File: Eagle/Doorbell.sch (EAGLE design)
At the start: 31 parts, among them U1 MIC2920A-3.3

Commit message: r1 - switching supply
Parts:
- removed C5: 470uF 25V, SparkFun-Capacitors:CAP_POLE
- removed U1: MIC2920A-3.3, Microchip_By_element14_Batch_1:MCP1790-3302E/DB
- added C8: 2.2uF, SparkFun-Passives:CAP1206
- added D5: BAT20J, SparkFun-DiscreteSemi:DIODE-SCHOTTKY-BAT20J
- added L1: 6.8uH, SparkFun-Passives:INDUCTOR1007
- added VREG: LMR16006YQ3DDCRQ1, CuriousTech:LMR16006YQ
- C1: value 0.1uF -> 10uF
- C4: value 10uF 16V -> 100uF; device SparkFun-Capacitors:CAP_POLC -> SparkFun-Passives:CAP_POLF80
- R4: value 5K6 -> 470
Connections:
- removed net N$1: C3.1, C5.+, C6.1, D1.C, D3.C, U1.VIN
- new net +24V: C3.1, C4.+, C8.1, D1.C, D3.C, VREG.VIN
- new net N$10: C6.2, VREG.CB
- new net N$7: C6.1, D5.C, L1.1, VREG.SW
- net 3V3: now also L1.2, VREG.FB; no longer C4.+, U1.VOUT
- net GND: now also C8.2, D5.A, VREG.GND; no longer C5.-, C6.2, U1.GND_(TAB), U1.GND_(TAB)_2
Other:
- moved on the sheet: C1, C4, C6, C7

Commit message: Add files via upload
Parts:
- removed X1: (no value), con-molex:KK-156-4
- added 3V3: MCP1755T-3302E/OT, Microchip_By_element14_Batch_1:MCP1801T-3302I/OT
- added C5: 0.1uF, SparkFun-Capacitors:CAP
- added D6, D7: (no value), SparkFun-DiscreteSemi:DIODESOD123
- added J2, J3: (no value), SparkFun-Connectors:M01SMDNS
- added L2: (no value), SparkFun-Passives:INDUCTOR0805
- added Q1: MOSFET-NCHANNEL, SparkFun-DiscreteSemi:MOSFET-NCHANNELAO3404A
- added R9: 1K, SparkFun-Resistors:RESISTOR0805-RES
- added U$6, U$7: SMD-PAD-SM, CuriousTech:SMD-PAD-SM
- added X2: 1751251, con-phoenix-350:1751251
- C1: value 10uF -> (none); device SparkFun-Capacitors:CAP -> SparkFun-Capacitors:CAP_POLPTH4
- C2: value 1uF -> 2.2uF; device SparkFun-Capacitors:CAP -> SparkFun-Passives:CAP1206
- C3: value 0.1uF -> 10uF
- C4: value 100uF -> 0.1uF; device SparkFun-Passives:CAP_POLF80 -> SparkFun-Capacitors:CAP
- C8: value 2.2uF -> 1uF; device SparkFun-Passives:CAP1206 -> SparkFun-Capacitors:CAP
- L1: value 6.8uH -> (none); device SparkFun-Passives:INDUCTOR1007 -> SparkFun-Passives:INDUCTOR0805
- R4: value 470 -> 1K
- R5, R6: value 10K -> 4K7
- VREG: value LMR16006YQ3DDCRQ1 -> LMR16006YQ5DDCRQ1
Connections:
- net IO5 renamed DB
- new net 5V: 3V3.VIN, 3V3.~SHDN, C3.1, C7.1, D6.C, L1.2, L2.2, U$7.P$1, VREG.FB, _.8
- new net N$1: D6.A, D7.A, Q1.D, U$6.P$1
- new net N$8: Q1.G, R9.2
- net +24V: now also C1.+, C2.1, C4.1, D7.C, U$3.P$1; no longer C3.1, C4.+, C8.1
- net 3V3: now also 3V3.VOUT, C5.1, _.7; no longer C1.1, C7.1, L1.2, U$3.P$1, VREG.FB, _.6, _.8
- net GND: now also 3V3.VSS, C1.-, C2.2, C4.2, C5.2, Q1.S, _.3; no longer C1.2, C4.-, C8.2, _.7
- net IO12: now also _.5; no longer _.4
- net IO13: now also _.6; no longer _.5
- net IO14: now also _.4; no longer _.3
- net IO15: now also R9.1
- net J1: now also C8.2, X2-2.K; no longer C2.2, X1-3.S
- net N$2: now also C8.1; no longer C2.1
- net N$3: now also J2.1, X2-1.K; no longer X1-1.S, X1-2.S
- net N$5: now also J3.1, X2-3.K; no longer X1-4.S
- net N$7: now also L2.1
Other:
- note added: "<--- 100-200 ohm, 5W resistor --->"
- note added: "<-Use only one!->"
- moved on the sheet: ., C2, C3, C6, C7, C8, D1, D2, D3, D4, D5, DS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

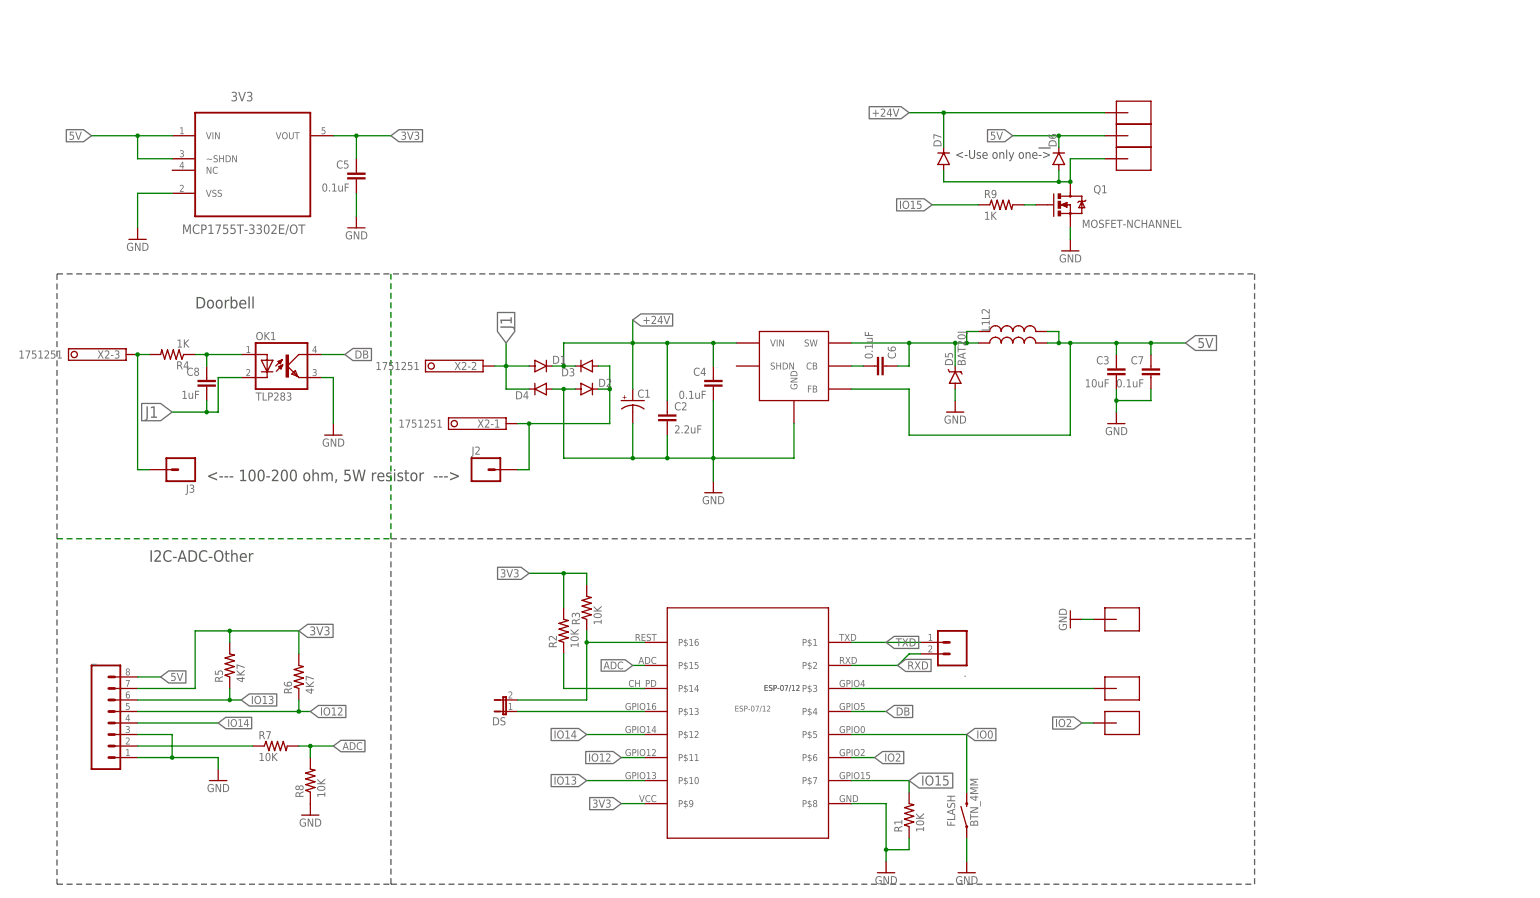
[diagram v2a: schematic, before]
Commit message: Added the inline diode
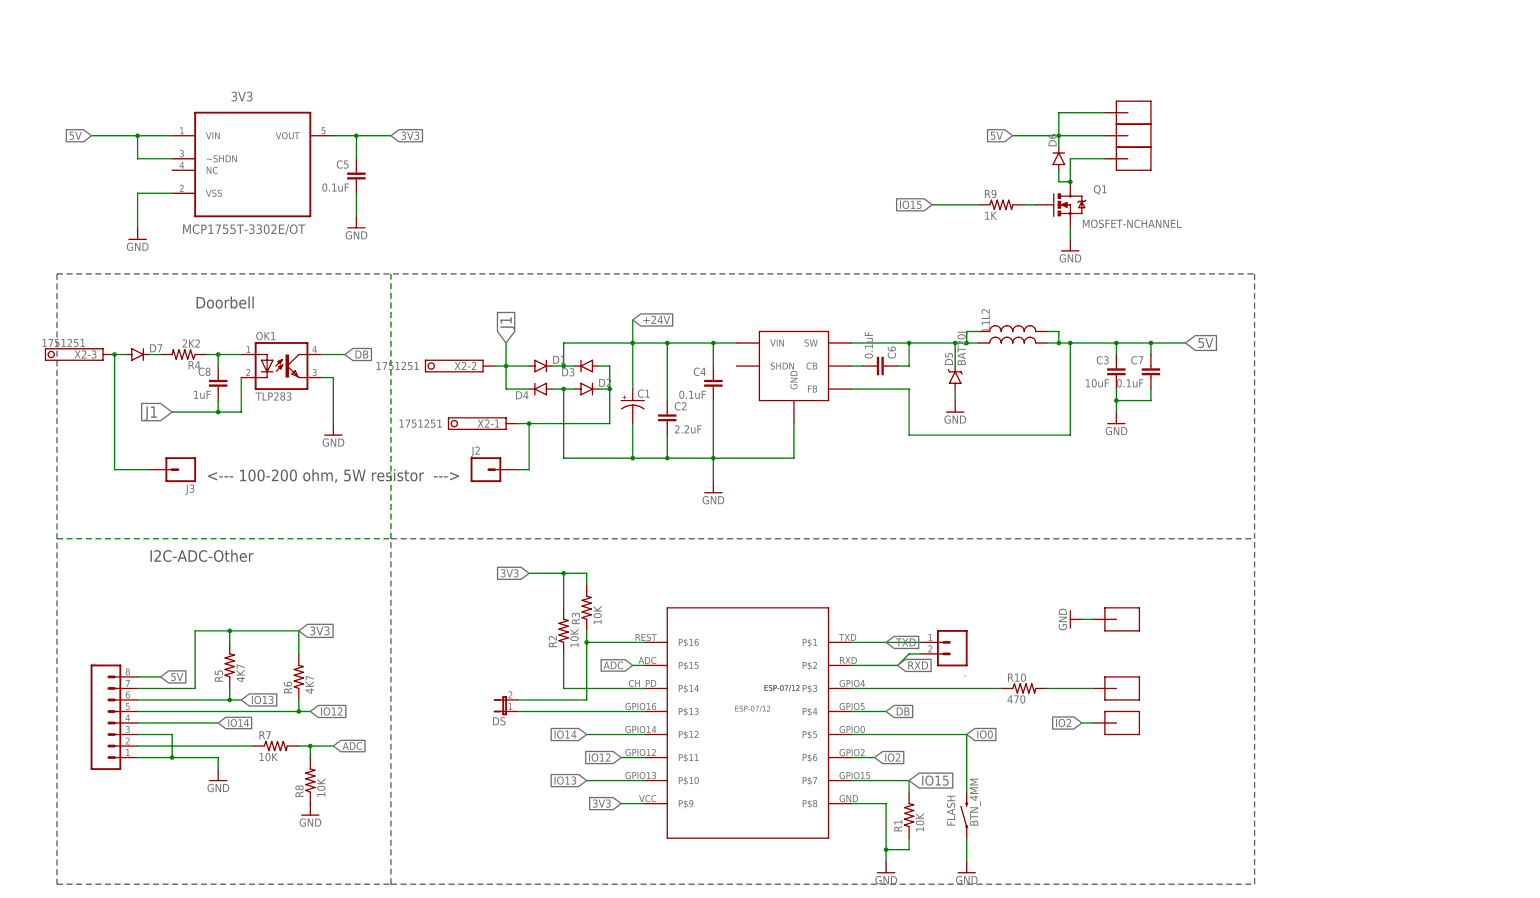
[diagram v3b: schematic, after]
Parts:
- added R10: 470, SparkFun-Resistors:RESISTOR0805-RES
- R4: value 1K -> 2K2
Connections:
- new net N$12: R10.2, U$2.P$1
- new net N$13: D7.C, R4.2
- net +24V: no longer D7.C, U$3.P$1
- net 5V: now also U$3.P$1
- net N$1: no longer D7.A
- net N$5: now also D7.A; no longer R4.2
- net N$6: now also R10.1; no longer U$2.P$1
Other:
- note removed: "<-Use only one!->"
- moved on the sheet: C8, D7, R4, X2-3
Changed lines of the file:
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@@
 <part name="C4" library="SparkFun-Capacitors" deviceset="CAP" device="" value="0.1uF"/>
 <part name="GND7" library="supply1" deviceset="GND" device=""/>
-<part name="R4" library="SparkFun-Resistors" deviceset="RESISTOR" device="0805-RES" value="1K"/>
+<part name="R4" library="SparkFun-Resistors" deviceset="RESISTOR" device="0805-RES" value="2K2"/>
 <part name="FLASH" library="CuriousTech" deviceset="BTN_4MM" device=""/>
 <part name="GND3" library="supply1" deviceset="GND" device=""/>
@@
 <part name="J3" library="SparkFun-Connectors" deviceset="M01" device="SMDNS"/>
 <part name="D6" library="SparkFun-DiscreteSemi" deviceset="DIODE" device="SOD123"/>
-<part name="D7" library="SparkFun-DiscreteSemi" deviceset="DIODE" device="SOD123"/>
 <part name="U$3" library="CuriousTech" deviceset="SMD-PAD-SM" device=""/>
 <part name="C8" library="SparkFun-Capacitors" deviceset="CAP" device="" value="1uF"/>
+<part name="R10" library="SparkFun-Resistors" deviceset="RESISTOR" device="0805-RES" value="470"/>
+<part name="D7" library="SparkFun-DiscreteSemi" deviceset="DIODE" device="SOD123"/>
 </parts>
 <sheets>
@@
 <text x="20.32" y="71.12" size="2.54" layer="97" font="vector">I2C-ADC-Other</text>
 <text x="30.48" y="127" size="2.54" layer="97">Doorbell</text>
-<text x="198.12" y="160.02" size="1.9304" layer="97">&lt;-Use only one!-&gt;</text>
 <text x="33.02" y="88.9" size="2.54" layer="97">&lt;--- 100-200 ohm, 5W resistor  ---&gt;</text>
 </plain>
@@
 <attribute name="VALUE" x="38.1" y="20.32" size="1.778" layer="96" rot="MR0"/>
 </instance>
-<instance part="R4" gate="G$1" x="25.4" y="116.84" smashed="yes" rot="R180">
-<attribute name="NAME" x="29.21" y="115.3414" size="1.778" layer="95" rot="R180"/>
-<attribute name="VALUE" x="29.21" y="120.142" size="1.778" layer="96" rot="R180"/>
+<instance part="R4" gate="G$1" x="27.94" y="116.84" smashed="yes" rot="R180">
+<attribute name="NAME" x="31.75" y="115.3414" size="1.778" layer="95" rot="R180"/>
+<attribute name="VALUE" x="31.75" y="120.142" size="1.778" layer="96" rot="R180"/>
 </instance>
 <instance part="FLASH" gate="G$1" x="200.66" y="15.24" smashed="yes" rot="R90">
@@
 <attribute name="VALUE" x="80.01" y="115.189" size="1.778" layer="96" rot="R180"/>
 </instance>
-<instance part="X2" gate="-3" x="15.24" y="116.84" smashed="yes" rot="R180">
-<attribute name="NAME" x="13.97" y="117.729" size="1.778" layer="95" rot="R180"/>
-<attribute name="VALUE" x="1.27" y="117.729" size="1.778" layer="96" rot="R180"/>
+<instance part="X2" gate="-3" x="10.16" y="116.84" smashed="yes" rot="R180">
+<attribute name="NAME" x="8.89" y="117.729" size="1.778" layer="95" rot="R180"/>
+<attribute name="VALUE" x="6.35" y="120.269" size="1.778" layer="96" rot="R180"/>
 </instance>
 <instance part="Q1" gate="G$1" x="223.52" y="149.86" smashed="yes">
@@
 <attribute name="VALUE" x="223.2914" y="162.56" size="1.778" layer="96" rot="R90"/>
 </instance>
-<instance part="D7" gate="G$1" x="195.58" y="160.02" smashed="yes" rot="R90">
-<attribute name="NAME" x="195.0974" y="162.56" size="1.778" layer="95" rot="R90"/>
-<attribute name="VALUE" x="197.8914" y="162.56" size="1.778" layer="96" rot="R90"/>
-</instance>
 <instance part="U$3" gate="G$1" x="236.22" y="170.18" smashed="yes"/>
-<instance part="C8" gate="G$1" x="33.02" y="109.22" smashed="yes" rot="MR0">
-<attribute name="NAME" x="31.496" y="112.141" size="1.778" layer="95" rot="MR0"/>
-<attribute name="VALUE" x="31.496" y="107.061" size="1.778" layer="96" rot="MR0"/>
+<instance part="C8" gate="G$1" x="35.56" y="109.22" smashed="yes" rot="MR0">
+<attribute name="NAME" x="34.036" y="112.141" size="1.778" layer="95" rot="MR0"/>
+<attribute name="VALUE" x="34.036" y="107.061" size="1.778" layer="96" rot="MR0"/>
+</instance>
+<instance part="R10" gate="G$1" x="213.36" y="43.18" smashed="yes">
+<attribute name="NAME" x="209.55" y="44.6786" size="1.778" layer="95"/>
+<attribute name="VALUE" x="209.55" y="39.878" size="1.778" layer="96"/>
+</instance>
+<instance part="D7" gate="G$1" x="17.78" y="116.84" smashed="yes">
+<attribute name="NAME" x="20.32" y="117.3226" size="1.778" layer="95"/>
+<attribute name="VALUE" x="20.32" y="114.5286" size="1.778" layer="96"/>
 </instance>
 </instances>
@@
 <label x="127" y="124.46" size="1.778" layer="95" xref="yes"/>
 </segment>
-<segment>
-<pinref part="D7" gate="G$1" pin="C"/>
-<wire x1="195.58" y1="162.56" x2="195.58" y2="170.18" width="0.1524" layer="91"/>
-<label x="187.96" y="170.18" size="1.778" layer="95" rot="R180" xref="yes"/>
-<pinref part="U$3" gate="G$1" pin="P$1"/>
-<wire x1="195.58" y1="170.18" x2="187.96" y2="170.18" width="0.1524" layer="91"/>
-<wire x1="231.14" y1="170.18" x2="195.58" y2="170.18" width="0.1524" layer="91"/>
-<junction x="195.58" y="170.18"/>
-</segment>
 </net>
 <net name="N$3" class="0">
@@
 <net name="N$5" class="0">
 <segment>
-<pinref part="R4" gate="G$1" pin="2"/>
-<wire x1="17.78" y1="116.84" x2="20.32" y2="116.84" width="0.1524" layer="91"/>
 <pinref part="X2" gate="-3" pin="K"/>
 <pinref part="J3" gate="G$1" pin="1"/>
-<wire x1="20.32" y1="91.44" x2="17.78" y2="91.44" width="0.1524" layer="91"/>
-<wire x1="17.78" y1="91.44" x2="17.78" y2="116.84" width="0.1524" layer="91"/>
-<junction x="17.78" y="116.84"/>
+<wire x1="20.32" y1="91.44" x2="12.7" y2="91.44" width="0.1524" layer="91"/>
+<wire x1="12.7" y1="91.44" x2="12.7" y2="116.84" width="0.1524" layer="91"/>
+<pinref part="D7" gate="G$1" pin="A"/>
+<wire x1="12.7" y1="116.84" x2="15.24" y2="116.84" width="0.1524" layer="91"/>
+<junction x="12.7" y="116.84"/>
 </segment>
 </net>
@@
 </segment>
 <segment>
-<wire x1="40.64" y1="111.76" x2="35.56" y2="111.76" width="0.1524" layer="91"/>
-<wire x1="35.56" y1="111.76" x2="35.56" y2="104.14" width="0.1524" layer="91"/>
-<wire x1="35.56" y1="104.14" x2="33.02" y2="104.14" width="0.1524" layer="91"/>
+<wire x1="40.64" y1="111.76" x2="40.64" y2="104.14" width="0.1524" layer="91"/>
+<wire x1="40.64" y1="104.14" x2="35.56" y2="104.14" width="0.1524" layer="91"/>
 <label x="25.4" y="104.14" size="2.54" layer="95" rot="R180" xref="yes"/>
 <pinref part="OK1" gate="G$1" pin="C"/>
 <pinref part="C8" gate="G$1" pin="2"/>
-<wire x1="33.02" y1="104.14" x2="25.4" y2="104.14" width="0.1524" layer="91"/>
-<wire x1="33.02" y1="106.68" x2="33.02" y2="104.14" width="0.1524" layer="91"/>
-<junction x="33.02" y="104.14"/>
+<wire x1="35.56" y1="104.14" x2="25.4" y2="104.14" width="0.1524" layer="91"/>
+<wire x1="35.56" y1="106.68" x2="35.56" y2="104.14" width="0.1524" layer="91"/>
+<junction x="35.56" y="104.14"/>
 </segment>
 </net>
@@
 <segment>
 <pinref part="R4" gate="G$1" pin="1"/>
-<wire x1="30.48" y1="116.84" x2="33.02" y2="116.84" width="0.1524" layer="91"/>
+<wire x1="33.02" y1="116.84" x2="35.56" y2="116.84" width="0.1524" layer="91"/>
 <pinref part="OK1" gate="G$1" pin="A"/>
 <pinref part="C8" gate="G$1" pin="1"/>
-<wire x1="33.02" y1="116.84" x2="40.64" y2="116.84" width="0.1524" layer="91"/>
-<wire x1="33.02" y1="114.3" x2="33.02" y2="116.84" width="0.1524" layer="91"/>
-<junction x="33.02" y="116.84"/>
+<wire x1="35.56" y1="116.84" x2="40.64" y2="116.84" width="0.1524" layer="91"/>
+<wire x1="35.56" y1="114.3" x2="35.56" y2="116.84" width="0.1524" layer="91"/>
+<junction x="35.56" y="116.84"/>
 </segment>
 </net>
@@
 <wire x1="129.54" y1="48.26" x2="127" y2="48.26" width="0.1524" layer="91"/>
 <label x="127" y="48.26" size="1.6764" layer="95" rot="R180" xref="yes"/>
-</segment>
-</net>
-<net name="N$6" class="0">
-<segment>
-<pinref part="U$1" gate="G$1" pin="P$3"/>
-<wire x1="175.26" y1="43.18" x2="228.6" y2="43.18" width="0.1524" layer="91"/>
-<pinref part="U$2" gate="G$1" pin="P$1"/>
 </segment>
 </net>
@@
 <wire x1="220.98" y1="154.94" x2="223.52" y2="154.94" width="0.1524" layer="91"/>
 <junction x="223.52" y="154.94"/>
-<pinref part="D7" gate="G$1" pin="A"/>
-<wire x1="195.58" y1="157.48" x2="195.58" y2="154.94" width="0.1524" layer="91"/>
-<wire x1="195.58" y1="154.94" x2="220.98" y2="154.94" width="0.1524" layer="91"/>
-<junction x="220.98" y="154.94"/>
 </segment>
 </net>
@@
 <wire x1="220.98" y1="162.56" x2="220.98" y2="165.1" width="0.1524" layer="91"/>
 <junction x="220.98" y="165.1"/>
+<pinref part="U$3" gate="G$1" pin="P$1"/>
+<wire x1="231.14" y1="170.18" x2="220.98" y2="170.18" width="0.1524" layer="91"/>
+<wire x1="220.98" y1="170.18" x2="220.98" y2="165.1" width="0.1524" layer="91"/>
 </segment>
 </net>
@@
 <segment>
 <pinref part="OK1" gate="G$1" pin="COL"/>
+<label x="63.5" y="116.84" size="1.778" layer="95" xref="yes"/>
 <wire x1="58.42" y1="116.84" x2="63.5" y2="116.84" width="0.1524" layer="91"/>
-<label x="63.5" y="116.84" size="1.778" layer="95" xref="yes"/>
-</segment>
-</net>
+</segment>
+</net>
+<net name="N$6" class="0">
+<segment>
+<pinref part="U$1" gate="G$1" pin="P$3"/>
+<pinref part="R10" gate="G$1" pin="1"/>
+<wire x1="175.26" y1="43.18" x2="208.28" y2="43.18" width="0.1524" layer="91"/>
+</segment>
+</net>
+<net name="N$12" class="0">
+<segment>
+<pinref part="R10" gate="G$1" pin="2"/>
+<pinref part="U$2" gate="G$1" pin="P$1"/>
+<wire x1="218.44" y1="43.18" x2="228.6" y2="43.18" width="0.1524" layer="91"/>
+</segment>
+</net>
+<net name="N$13" class="0">
+<segment>
+<pinref part="D7" gate="G$1" pin="C"/>
+<pinref part="R4" gate="G$1" pin="2"/>
+<wire x1="20.32" y1="116.84" x2="22.86" y2="116.84" width="0.1524" layer="91"/>
+</segment>
+</net>
